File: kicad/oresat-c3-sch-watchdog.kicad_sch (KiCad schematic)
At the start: 35 parts, among them U28 TLV1704AIPWR

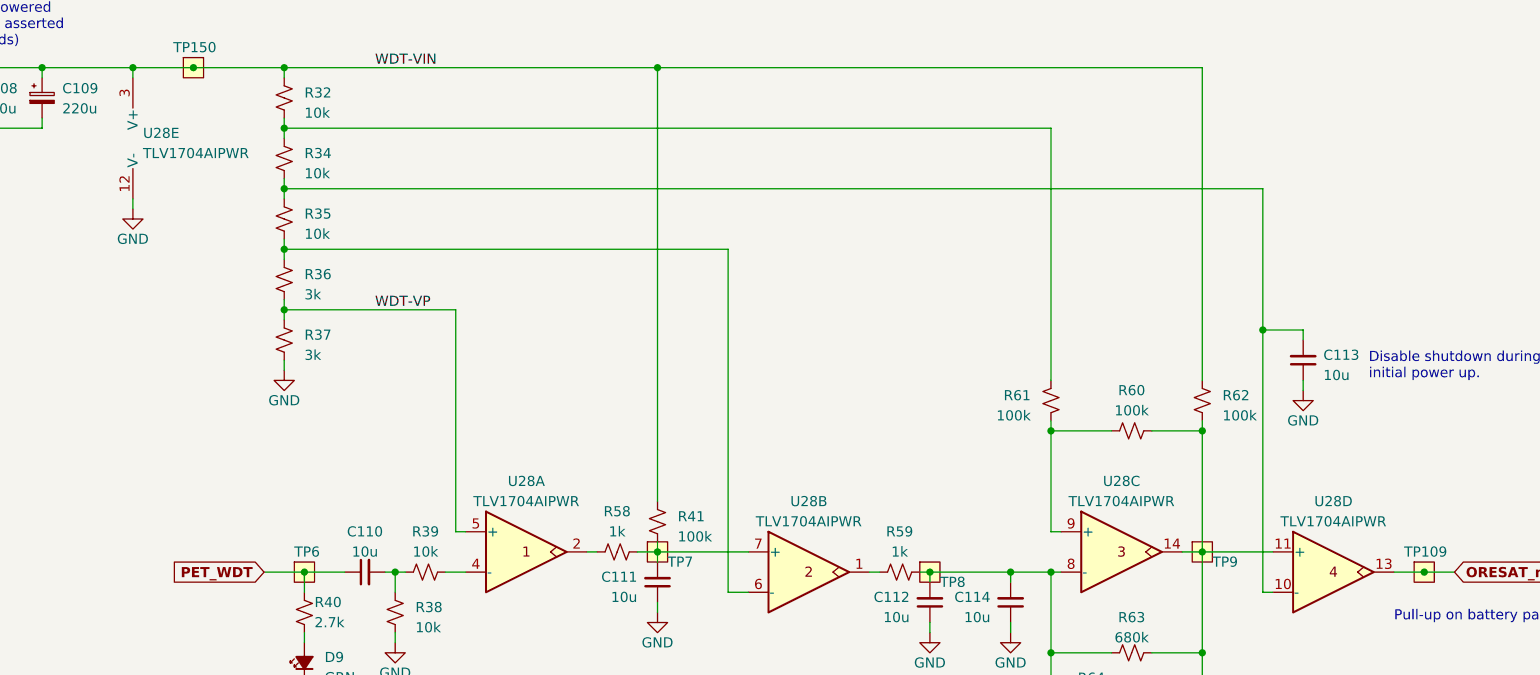
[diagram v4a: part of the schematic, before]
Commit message: An evening of cleanups from the design review. Includes lots of ERC and DRC cleanup, although still over 450 DRC errors mostly from RF keepouts. Fixed PA ground connection, notes on pin reset configuration, and lots of small naggy things. Also cleaned up wierd broken traces on eMMC traces. No longer all same length (sorry Oliver) but it shouldn't affect performance.
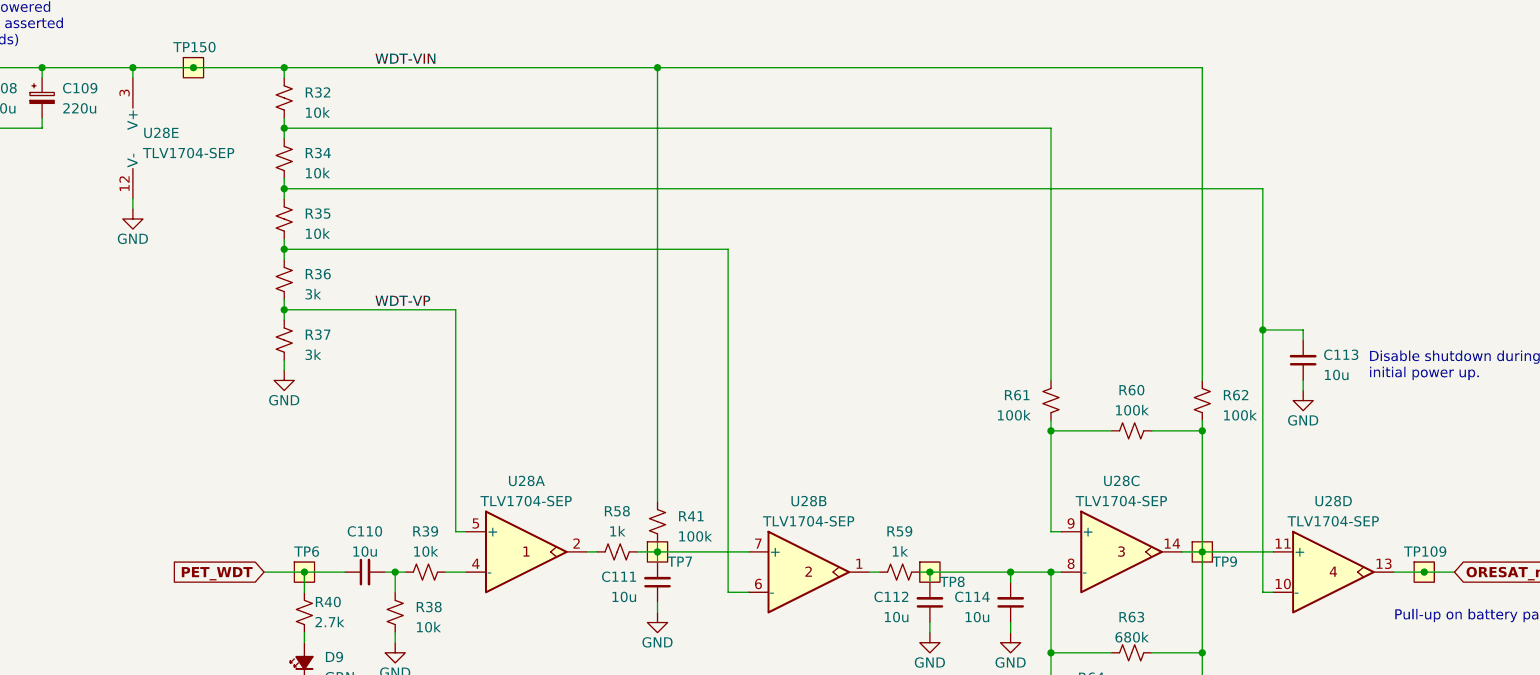
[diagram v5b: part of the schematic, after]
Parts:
- U28: value TLV1704AIPWR -> TLV1704-SEP
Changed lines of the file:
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@@
       (effects (font (size 1.27 1.27)))
     )
-    (property "Value" "TLV1704AIPWR" (at 280.67 156.21 0)
+    (property "Value" "TLV1704-SEP" (at 280.67 156.21 0)
       (effects (font (size 1.27 1.27)))
     )
@@
       (effects (font (size 1.27 1.27)) hide)
     )
-    (property "Datasheet" "https://www.ti.com/lit/ds/symlink/tlv1704.pdf" (at 280.67 181.356 0)
+    (property "Datasheet" "https://www.ti.com/lit/ds/symlink/tlv1704-sep.pdf" (at 280.67 181.356 0)
       (effects (font (size 1.27 1.27)) hide)
     )
@@
       (effects (font (size 1.27 1.27)))
     )
-    (property "Value" "TLV1704AIPWR" (at 241.3 158.75 0)
+    (property "Value" "TLV1704-SEP" (at 241.3 158.75 0)
       (effects (font (size 1.27 1.27)))
     )
@@
       (effects (font (size 1.27 1.27)) hide)
     )
-    (property "Datasheet" "https://www.ti.com/lit/ds/symlink/tlv1704.pdf" (at 241.3 183.896 0)
+    (property "Datasheet" "https://www.ti.com/lit/ds/symlink/tlv1704-sep.pdf" (at 241.3 183.896 0)
       (effects (font (size 1.27 1.27)) hide)
     )
@@
       (effects (font (size 1.27 1.27)) (justify left))
     )
-    (property "Value" "TLV1704AIPWR" (at 157.48 112.395 0)
+    (property "Value" "TLV1704-SEP" (at 157.48 112.395 0)
       (effects (font (size 1.27 1.27)) (justify left))
     )
@@
       (effects (font (size 1.27 1.27)) hide)
     )
-    (property "Datasheet" "https://www.ti.com/lit/ds/symlink/tlv1704.pdf" (at 158.75 129.286 0)
+    (property "Datasheet" "https://www.ti.com/lit/ds/symlink/tlv1704-sep.pdf" (at 158.75 129.286 0)
       (effects (font (size 1.27 1.27)) hide)
     )
@@
       (effects (font (size 1.27 1.27)))
     )
-    (property "Value" "TLV1704AIPWR" (at 205.74 156.21 0)
+    (property "Value" "TLV1704-SEP" (at 205.74 156.21 0)
       (effects (font (size 1.27 1.27)))
     )
@@
       (effects (font (size 1.27 1.27)) hide)
     )
-    (property "Datasheet" "https://www.ti.com/lit/ds/symlink/tlv1704.pdf" (at 205.74 181.356 0)
+    (property "Datasheet" "https://www.ti.com/lit/ds/symlink/tlv1704-sep.pdf" (at 205.74 181.356 0)
       (effects (font (size 1.27 1.27)) hide)
     )
@@
       (effects (font (size 1.27 1.27)))
     )
-    (property "Value" "TLV1704AIPWR" (at 307.34 158.75 0)
+    (property "Value" "TLV1704-SEP" (at 307.34 158.75 0)
       (effects (font (size 1.27 1.27)))
     )
@@
       (effects (font (size 1.27 1.27)) hide)
     )
-    (property "Datasheet" "https://www.ti.com/lit/ds/symlink/tlv1704.pdf" (at 307.34 183.896 0)
-      (effects (font (size 1.27 1.27)) hide)
-    )
+    (property "Datasheet" "https://www.ti.com/lit/ds/symlink/tlv1704-sep.pdf" (at 307.34 183.896 0)
+      (effects (font (size 1.27 1.27)) hide)
+    )

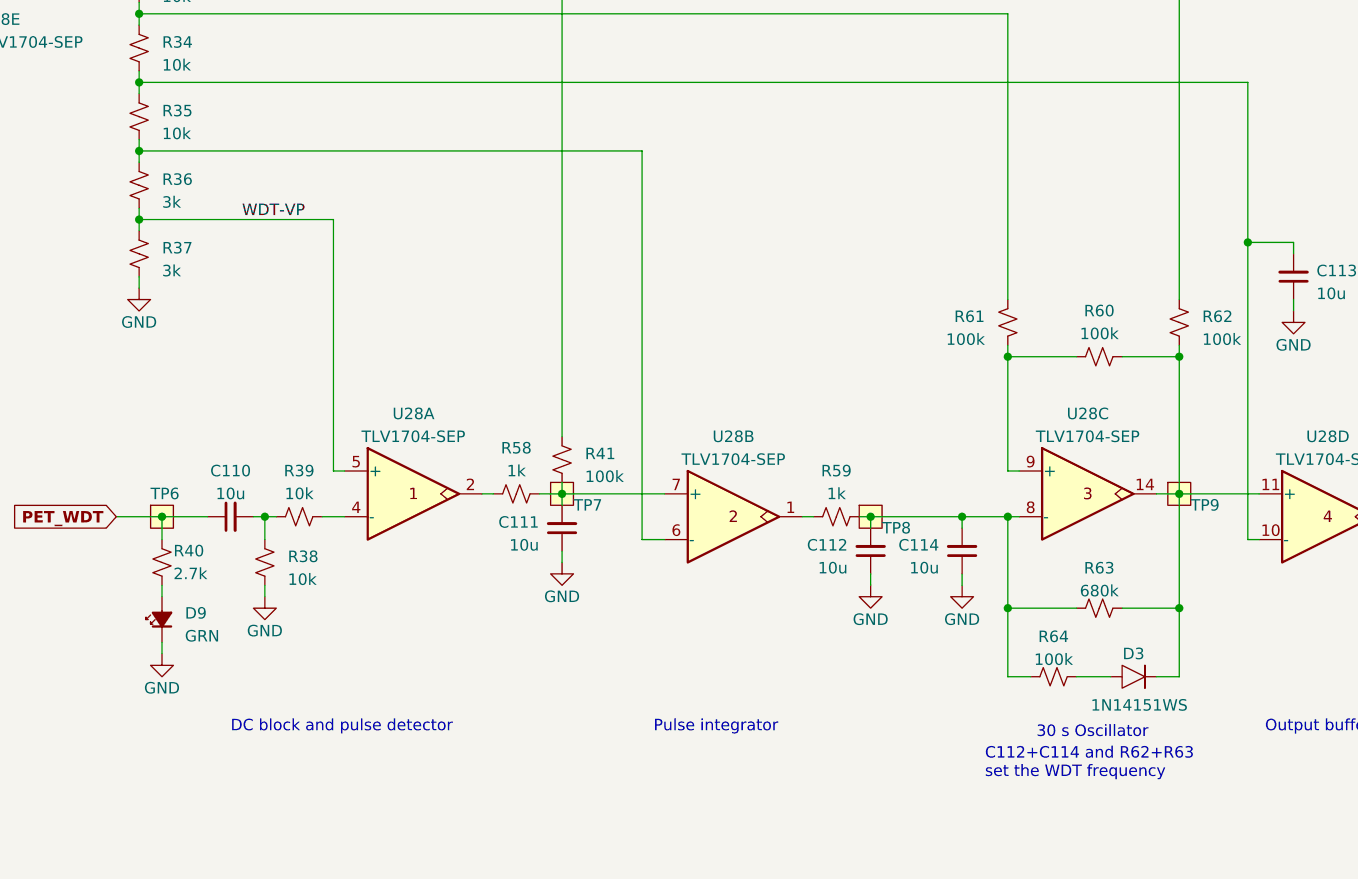
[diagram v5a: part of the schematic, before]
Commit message: First round of BOM fixes and optimizations.
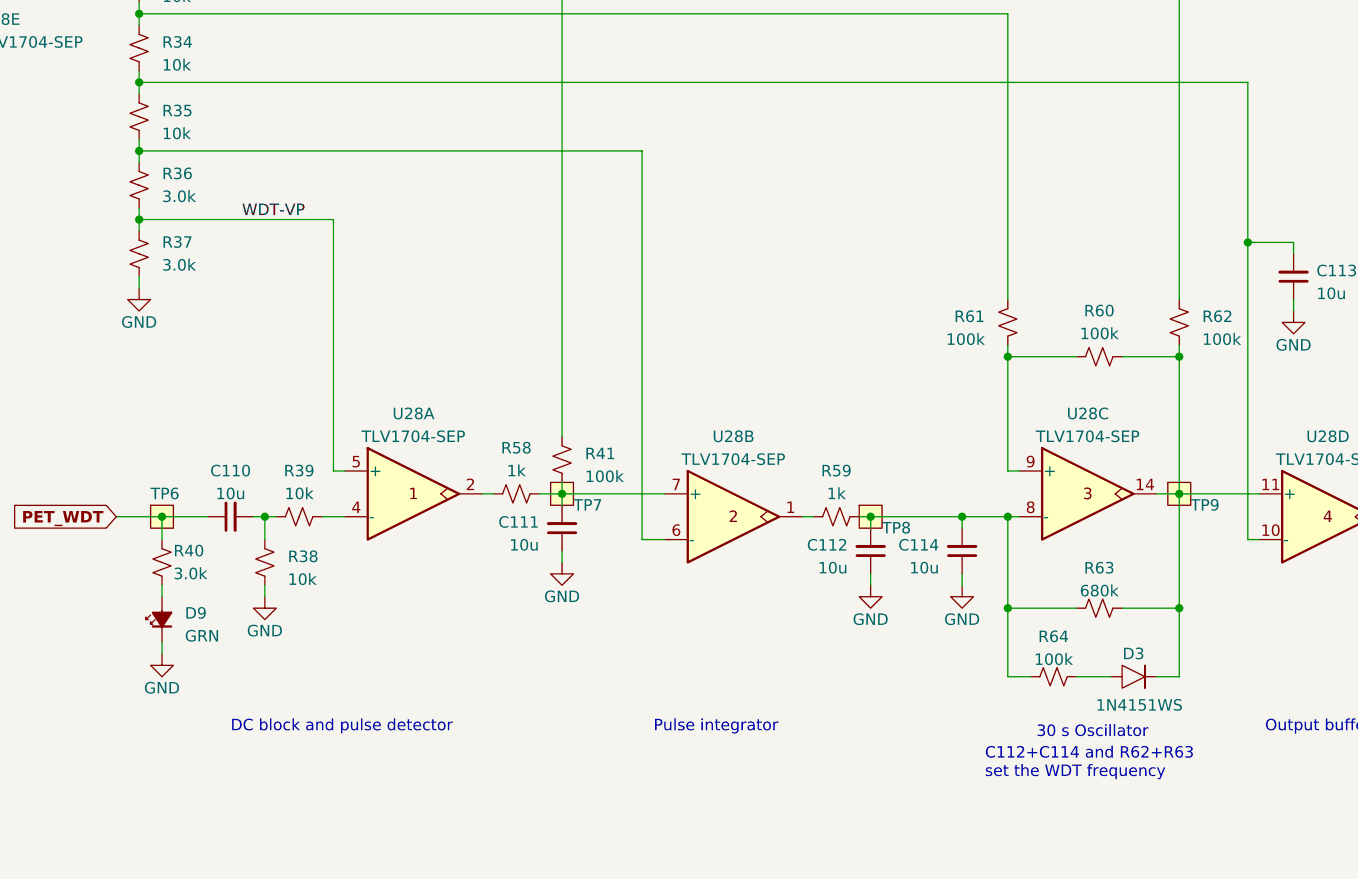
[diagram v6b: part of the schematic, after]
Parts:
- D3: value 1N14151WS -> 1N4151WS
- R36, R37: value 3k -> 3.0k
- R40: value 2.7k -> 3.0k
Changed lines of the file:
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@@
   (symbol (lib_id "Device:R_Small_US") (at 175.26 128.27 0) (unit 1)
     (in_bom yes) (on_board yes) (dnp no) (fields_autoplaced)
-    (property "Reference" "R36" (at 177.8 127.635 0)
-      (effects (font (size 1.27 1.27)) (justify left))
-    )
-    (property "Value" "3k" (at 177.8 130.175 0)
+    (property "Reference" "R36" (at 177.8 127 0)
+      (effects (font (size 1.27 1.27)) (justify left))
+    )
+    (property "Value" "3.0k" (at 177.8 129.54 0)
       (effects (font (size 1.27 1.27)) (justify left))
     )
@@
       (effects (font (size 1.27 1.27)))
     )
-    (property "Value" "1N14151WS" (at 286.385 186.055 0)
+    (property "Value" "1N4151WS" (at 286.385 186.055 0)
       (effects (font (size 1.27 1.27)))
     )
@@
       (effects (font (size 1.27 1.27)) (justify left))
     )
-    (property "Value" "2.7k" (at 179.07 171.45 0)
+    (property "Value" "3.0k" (at 179.07 171.45 0)
       (effects (font (size 1.27 1.27)) (justify left))
     )
@@
   (symbol (lib_id "Device:R_Small_US") (at 175.26 135.89 0) (unit 1)
     (in_bom yes) (on_board yes) (dnp no) (fields_autoplaced)
-    (property "Reference" "R37" (at 177.8 135.255 0)
-      (effects (font (size 1.27 1.27)) (justify left))
-    )
-    (property "Value" "3k" (at 177.8 137.795 0)
-      (effects (font (size 1.27 1.27)) (justify left))
-    )
+    (property "Reference" "R37" (at 177.8 134.62 0)
+      (effects (font (size 1.27 1.27)) (justify left))
+    )
+    (property "Value" "3.0k" (at 177.8 137.16 0)
+      (effects (font (size 1.27 1.27)) (justify left))
+    )

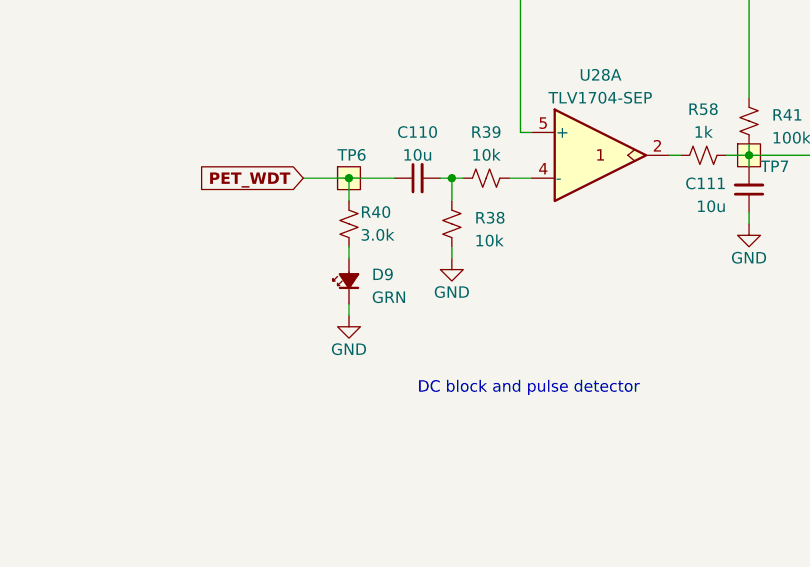
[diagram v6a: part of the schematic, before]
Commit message: Cleanup of crystals, more BOM reduction and fixes.
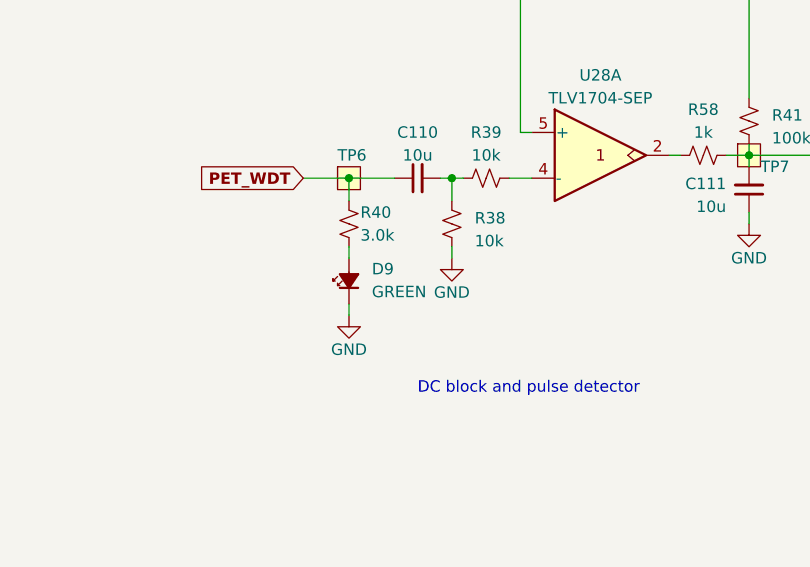
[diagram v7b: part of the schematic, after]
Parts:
- D9: value GRN -> GREEN
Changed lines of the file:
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@@
   (symbol (lib_id "Device:LED_Small_Filled") (at 177.8 176.53 90) (unit 1)
     (in_bom yes) (on_board yes) (dnp no) (fields_autoplaced)
-    (property "Reference" "D9" (at 180.34 175.8315 90)
+    (property "Reference" "D9" (at 180.34 175.1965 90)
       (effects (font (size 1.27 1.27)) (justify right))
     )
-    (property "Value" "GRN" (at 180.34 178.3715 90)
+    (property "Value" "GREEN" (at 180.34 177.7365 90)
       (effects (font (size 1.27 1.27)) (justify right))
     )

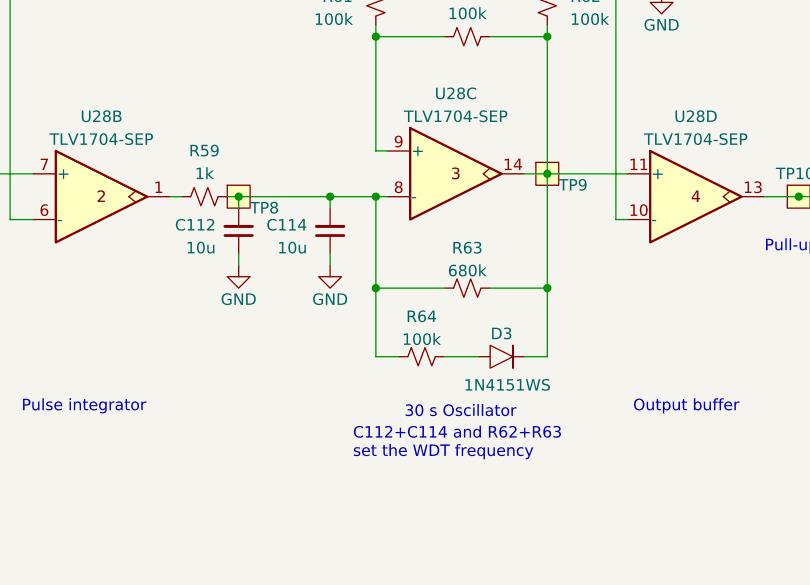
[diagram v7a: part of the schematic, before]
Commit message: Fixed R82 so that the damn thing doesn't reboot every two seconds. Fixed R63 to extend the watchdog timer. Fixed R83 and R84 in order to set the UVLO correctly.
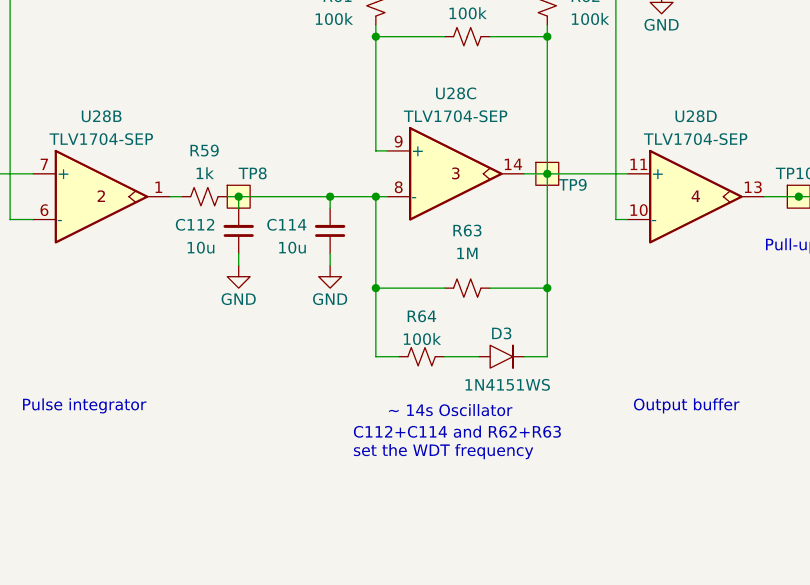
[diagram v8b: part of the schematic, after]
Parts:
- R63: value 680k -> 1M
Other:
- note added: "~ 14s Oscillator"
- note removed: "30 s Oscillator"
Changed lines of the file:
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@@
     (effects (font (size 1.27 1.27)) (justify left bottom))
   )
-  (text "30 s Oscillator" (at 274.955 189.865 0)
+  (text "~ 14s Oscillator" (at 273.05 189.865 0)
     (effects (font (size 1.27 1.27)) (justify left bottom))
   )
@@
   (symbol (lib_id "Device:R_Small_US") (at 281.94 175.26 270) (unit 1)
     (in_bom yes) (on_board yes) (dnp no) (fields_autoplaced)
-    (property "Reference" "R63" (at 281.94 170.815 90)
-      (effects (font (size 1.27 1.27)))
-    )
-    (property "Value" "680k" (at 281.94 173.355 90)
+    (property "Reference" "R63" (at 281.94 168.91 90)
+      (effects (font (size 1.27 1.27)))
+    )
+    (property "Value" "1M" (at 281.94 171.45 90)
       (effects (font (size 1.27 1.27)))
     )
@@
   (symbol (lib_id "oresat-misc:Test-Point-0.75mm-th") (at 256.54 165.1 0) (unit 1)
     (in_bom yes) (on_board yes) (dnp no)
-    (property "Reference" "TP8" (at 257.81 166.37 0)
-      (effects (font (size 1.27 1.27)) (justify left))
-    )
+    (property "Reference" "TP8" (at 256.54 162.56 0)
+      (effects (font (size 1.27 1.27)) (justify left))
+    )
